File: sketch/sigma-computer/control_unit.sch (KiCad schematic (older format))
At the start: 1 part

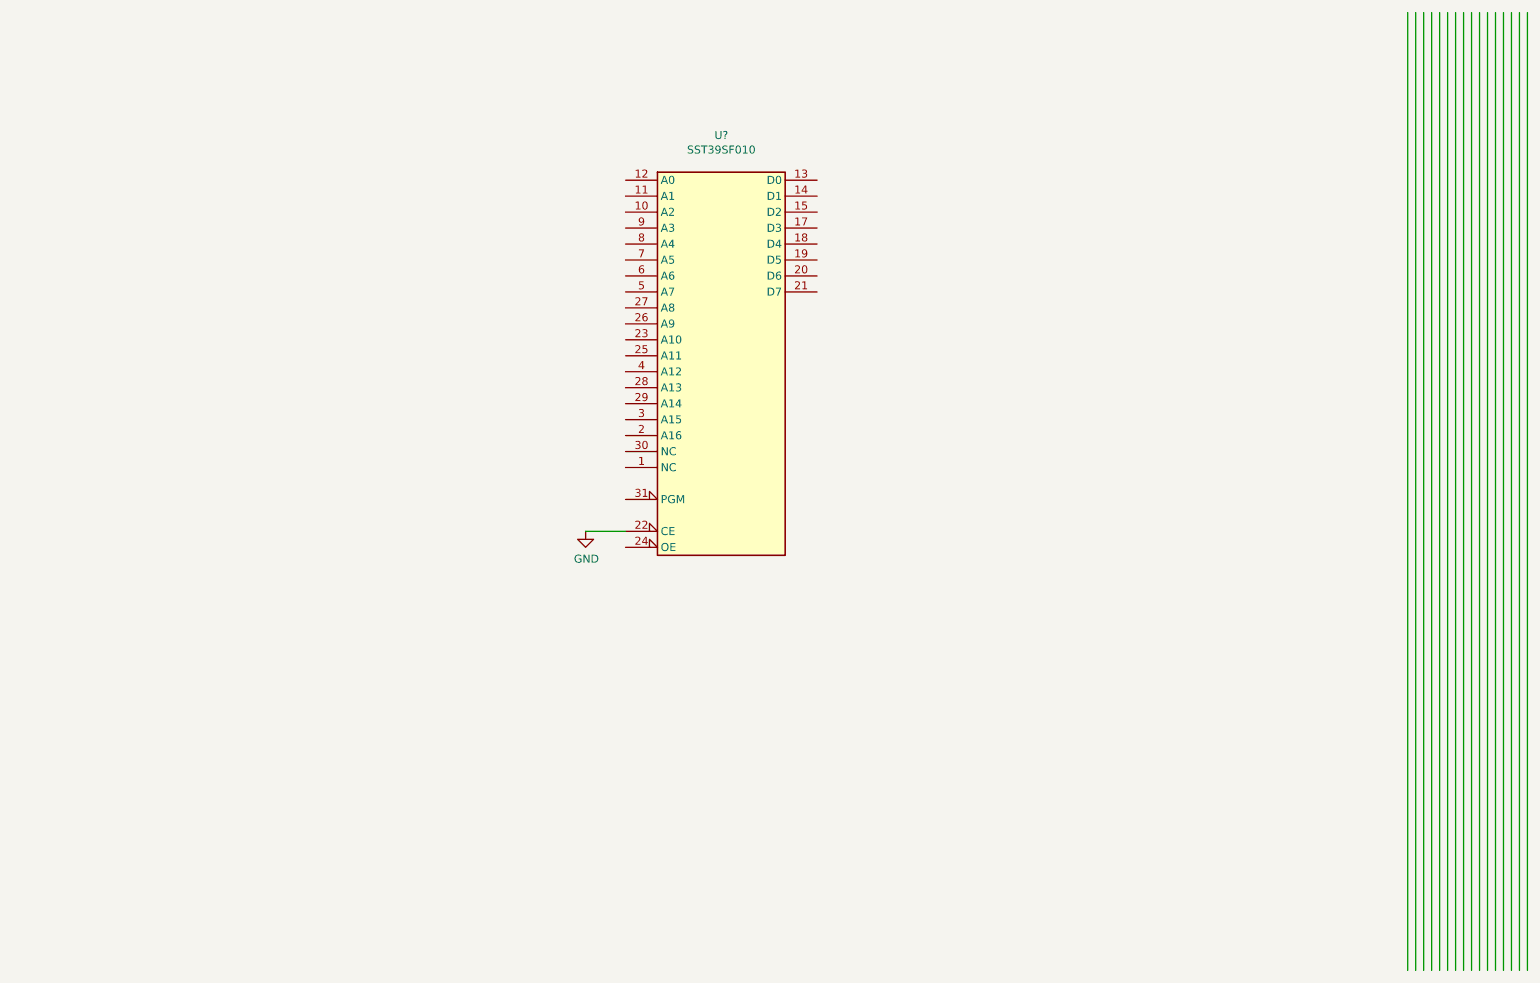
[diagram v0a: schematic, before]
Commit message: Started the microcode compiler
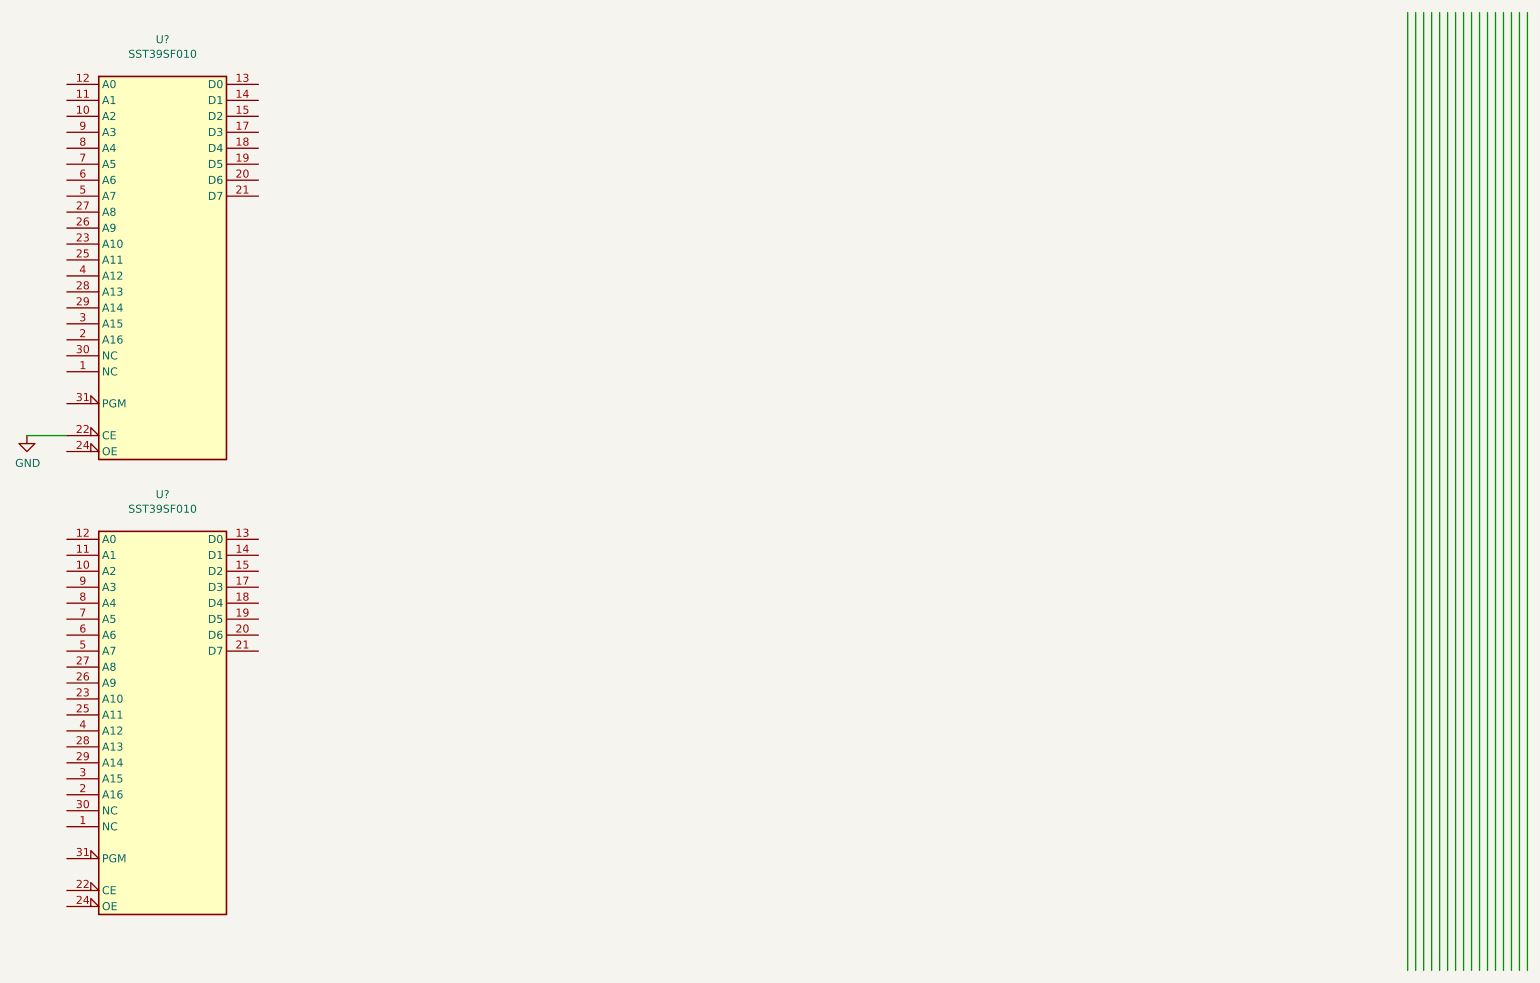
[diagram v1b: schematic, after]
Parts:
- added U?: SST39SF010, symbol Memory_Flash:SST39SF010
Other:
- moved on the sheet: U?
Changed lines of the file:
@@
 L Memory_Flash:SST39SF010 U?
 U 1 1 5D28F473
-P 6150 2750
-F 0 "U?" H 6150 4231 50  0000 C CNN
-F 1 "SST39SF010" H 6150 4140 50  0000 C CNN
-F 2 "" H 6150 3050 50  0001 C CNN
-F 3 "http://ww1.microchip.com/downloads/en/DeviceDoc/25022B.pdf" H 6150 3050 50  0001 C CNN
-	1    6150 2750
+P 2650 2150
+F 0 "U?" H 2650 3631 50  0000 C CNN
+F 1 "SST39SF010" H 2650 3540 50  0000 C CNN
+F 2 "" H 2650 2450 50  0001 C CNN
+F 3 "http://ww1.microchip.com/downloads/en/DeviceDoc/25022B.pdf" H 2650 2450 50  0001 C CNN
+	1    2650 2150
 	1    0    0    -1
 $EndComp
@@
 L power:GND #PWR?
 U 1 1 5D290CED
-P 5300 3750
-F 0 "#PWR?" H 5300 3500 50  0001 C CNN
-F 1 "GND" H 5305 3577 50  0000 C CNN
-F 2 "" H 5300 3750 50  0001 C CNN
-F 3 "" H 5300 3750 50  0001 C CNN
-	1    5300 3750
+P 1800 3150
+F 0 "#PWR?" H 1800 2900 50  0001 C CNN
+F 1 "GND" H 1805 2977 50  0000 C CNN
+F 2 "" H 1800 3150 50  0001 C CNN
+F 3 "" H 1800 3150 50  0001 C CNN
+	1    1800 3150
 	1    0    0    -1
 $EndComp
 Wire Wire Line
-	5300 3750 5550 3750
+	1800 3150 2050 3150
+$Comp
+L Memory_Flash:SST39SF010 U?
+U 1 1 5D2B77F7
+P 2650 5000
+F 0 "U?" H 2650 6481 50  0000 C CNN
+F 1 "SST39SF010" H 2650 6390 50  0000 C CNN
+F 2 "" H 2650 5300 50  0001 C CNN
+F 3 "http://ww1.microchip.com/downloads/en/DeviceDoc/25022B.pdf" H 2650 5300 50  0001 C CNN
+	1    2650 5000
+	1    0    0    -1
+$EndComp
 $EndSCHEMATC
